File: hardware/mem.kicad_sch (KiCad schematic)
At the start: 4 parts, among them U11 AS6C4008-55PCN, U6 74HC00, U7 AT28LV256

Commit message: Changed Ethernet Chip to Ethernet ModuleWIZ850IO
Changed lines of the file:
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@@
-		)
-	)
-	(label "Bank_{2}"
-		(at 93.98 111.76 0)
-		(effects
-			(font
-				(size 1.27 1.27)
-			)
-			(justify left bottom)
 		)
 	)
@@
 		)
 	)
-	(label "Bank_{0}"
-		(at 231.14 104.14 0)
-		(effects
-			(font
-				(size 1.27 1.27)
-			)
-			(justify left bottom)
-		)
-	)
 	(label "D1"
 		(at 199.39 66.04 180)
@@
 		)
 	)
-	(label "Bank_{1}"
-		(at 231.14 106.68 0)
-		(effects
-			(font
-				(size 1.27 1.27)
-			)
-			(justify left bottom)
-		)
-	)
 	(label "D0"
 		(at 62.23 106.68 180)
@@
 		)
 	)
-	(label "Bank_{0}"
-		(at 93.98 106.68 0)
-		(effects
-			(font
-				(size 1.27 1.27)
-			)
-			(justify left bottom)
-		)
-	)
 	(label "D7"
 		(at 167.64 81.28 0)
@@
 		)
 	)
-	(label "Bank_{1}"
-		(at 93.98 109.22 0)
-		(effects
-			(font
-				(size 1.27 1.27)
-			)
-			(justify left bottom)
-		)
-	)
 	(label "Addr5"
 		(at 143.51 76.2 180)
@@
 	(label "D6"
 		(at 167.64 78.74 0)
-		(effects
-			(font
-				(size 1.27 1.27)
-			)
-			(justify left bottom)
-		)
-	)
-	(label "Bank_{2}"
-		(at 231.14 109.22 0)
 		(effects
 			(font
@@
 		)
 	)
+	(hierarchical_label "Bank_{0}"
+		(shape input)
+		(at 231.14 104.14 0)
+		(effects
+			(font
+				(size 1.27 1.27)
+			)
+			(justify left)
+		)
+	)
+	(hierarchical_label "Bank_{1}"
+		(shape input)
+		(at 93.98 109.22 0)
+		(effects
+			(font
+				(size 1.27 1.27)
+			)
+			(justify left)
+		)
+	)
+	(hierarchical_label "Bank_{2}"
+		(shape input)
+		(at 93.98 111.76 0)
+		(effects
+			(font
+				(size 1.27 1.27)
+			)
+			(justify left)
+		)
+	)
+	(hierarchical_label "Bank_{2}"
+		(shape input)
+		(at 231.14 109.22 0)
+		(effects
+			(font
+				(size 1.27 1.27)
+			)
+			(justify left)
+		)
+	)
+	(hierarchical_label "Bank_{0}"
+		(shape input)
+		(at 93.98 106.68 0)
+		(effects
+			(font
+				(size 1.27 1.27)
+			)
+			(justify left)
+		)
+	)
+	(hierarchical_label "Bank_{1}"
+		(shape input)
+		(at 231.14 106.68 0)
+		(effects
+			(font
+				(size 1.27 1.27)
+			)
+			(justify left)
+		)
+	)

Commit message: Fixes and addres fix adding VDA AND VPA
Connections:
- net PHI2 renamed CLK
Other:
- moved on the sheet: U6E
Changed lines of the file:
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@@
 	)
 	(junction
+		(at 77.47 140.97)
+		(diameter 0)
+		(color 0 0 0 0)
+	)
+	(junction
 		(at 135.89 132.08)
 		(diameter 0)
@@
 	(wire
 		(pts
+			(xy 60.96 140.97) (xy 77.47 140.97)
+		)
+		(stroke
+			(width 0)
+			(type default)
+		)
+	)
+	(wire
+		(pts
 			(xy 93.98 109.22) (xy 90.17 109.22)
 		)
@@
 		)
 	)
+	(wire
+		(pts
+			(xy 77.47 140.97) (xy 77.47 142.24)
+		)
+		(stroke
+			(width 0)
+			(type default)
+		)
+	)
 	(bus
 		(pts
@@
 	(wire
 		(pts
-			(xy 77.47 139.7) (xy 77.47 142.24)
+			(xy 77.47 139.7) (xy 77.47 140.97)
 		)
 		(stroke
@@
 		)
 	)
+	(wire
+		(pts
+			(xy 60.96 132.08) (xy 60.96 140.97)
+		)
+		(stroke
+			(width 0)
+			(type default)
+		)
+	)
 	(bus
 		(pts
@@
 		)
 	)
-	(global_label "PHI2"
+	(global_label "CLK"
 		(shape input)
 		(at 212.09 138.43 180)
@@
 		)
 		(property "Intersheetrefs" "${INTERSHEET_REFS}"
-			(at 204.69 138.43 0)
+			(at 205.5367 138.43 0)
 			(effects
 				(font
@@
 		)
 	)
-	(global_label "PHI2"
+	(global_label "CLK"
 		(shape input)
 		(at 35.56 134.62 180)
@@
 		)
 		(property "Intersheetrefs" "${INTERSHEET_REFS}"
-			(at 28.16 134.62 0)
+			(at 29.0067 134.62 0)
 			(effects
 				(font
@@
 		)
 	)
-	(global_label "PHI2"
+	(global_label "CLK"
 		(shape input)
 		(at 35.56 139.7 180)
@@
 		)
 		(property "Intersheetrefs" "${INTERSHEET_REFS}"
-			(at 28.16 139.7 0)
+			(at 29.0067 139.7 0)
 			(effects
 				(font
@@
 		)
 	)
-	(global_label "PHI2"
+	(global_label "CLK"
 		(shape input)
 		(at 119.38 129.54 180)
@@
 		)
 		(property "Intersheetrefs" "${INTERSHEET_REFS}"
-			(at 111.98 129.54 0)
+			(at 112.8267 129.54 0)
 			(effects
 				(font
@@
 	(symbol
 		(lib_id "74xx:74HC00")
-		(at 257.81 120.65 90)
+		(at 265.43 139.7 0)
 		(unit 5)
 		(exclude_from_sim no)
@@
 		(fields_autoplaced yes)
 		(property "Reference" "U6"
-			(at 257.81 110.49 90)
+			(at 275.59 139.7 90)
 			(effects
 				(font
@@
 		)
 		(property "Value" "74HC00"
-			(at 257.81 113.03 90)
+			(at 273.05 139.7 90)
 			(effects
 				(font
@@
 		)
 		(property "Footprint" "Package_DIP:DIP-14_W7.62mm"
-			(at 257.81 120.65 0)
+			(at 265.43 139.7 0)
 			(effects
 				(font
@@
 		)
 		(property "Datasheet" "http://www.ti.com/lit/gpn/sn74hc00"
-			(at 257.81 120.65 0)
+			(at 265.43 139.7 0)
 			(effects
 				(font
@@
 		)
 		(property "Description" "quad 2-input NAND gate"
-			(at 257.81 120.65 0)
+			(at 265.43 139.7 0)
 			(effects
 				(font
@@
 	(symbol
 		(lib_id "power:GND")
-		(at 270.51 120.65 90)
+		(at 265.43 152.4 0)
 		(unit 1)
 		(exclude_from_sim no)
@@
 		(dnp no)
 		(property "Reference" "#PWR022"
-			(at 276.86 120.65 0)
+			(at 265.43 158.75 0)
 			(effects
 				(font
@@
 		)
 		(property "Value" "GND"
-			(at 275.59 120.65 0)
+			(at 265.43 157.48 0)
 			(effects
 				(font
@@
 		)
 		(property "Footprint" ""
-			(at 270.51 120.65 0)
+			(at 265.43 152.4 0)
 			(effects
 				(font
@@
 		)
 		(property "Datasheet" ""
-			(at 270.51 120.65 0)
+			(at 265.43 152.4 0)
 			(effects
 				(font
@@
 		)
 		(property "Description" "Power symbol creates a global label with name \"GND\" , ground"
-			(at 270.51 120.65 0)
+			(at 265.43 152.4 0)
 			(effects
 				(font
@@
 	(symbol
 		(lib_id "power:+3.3V")
-		(at 142.24 104.14 90)
+		(at 142.24 104.14 0)
 		(unit 1)
 		(exclude_from_sim no)
@@
 		(dnp no)
 		(property "Reference" "#PWR024"
-			(at 146.05 104.14 0)
+			(at 142.24 107.95 0)
 			(effects
 				(font
@@
 		)
 		(property "Value" "+3.3V"
-			(at 137.16 104.14 90)
+			(at 141.986 100.584 0)
 			(effects
 				(font
@@
 	)
 	(symbol
-		(lib_id "power:GND")
-		(at 60.96 132.08 270)
-		(unit 1)
-		(exclude_from_sim no)
-		(in_bom yes)
-		(on_board yes)
-		(dnp no)
-		(fields_autoplaced yes)
-		(property "Reference" "#PWR04"
-			(at 54.61 132.08 0)
-			(effects
-				(font
-					(size 1.27 1.27)
-				)
-				(hide yes)
-			)
-		)
-		(property "Value" "GND"
-			(at 57.15 132.0799 90)
-			(effects
-				(font
-					(size 1.27 1.27)
-				)
-				(justify right)
-			)
-		)
-		(property "Footprint" ""
-			(at 60.96 132.08 0)
-			(effects
-				(font
-					(size 1.27 1.27)
-				)
-				(hide yes)
-			)
-		)
-		(property "Datasheet" ""
-			(at 60.96 132.08 0)
-			(effects
-				(font
-					(size 1.27 1.27)
-				)
-				(hide yes)
-			)
-		)
-		(property "Description" "Power symbol creates a global label with name \"GND\" , ground"
-			(at 60.96 132.08 0)
-			(effects
-				(font
-					(size 1.27 1.27)
-				)
-				(hide yes)
-			)
-		)
-		(pin "1"
-		)
-		(instances
-			(project "Lambda One"
-				(path "/73ea9964-373f-4fdc-b03e-f532cf836c0d/393dc2fd-ccc9-40ef-ba1b-4142573d9a3b"
-					(reference "#PWR04")
-					(unit 1)
-				)
-			)
-		)
-	)
-	(symbol
 		(lib_id "74xx:74HC00")
 		(at 43.18 137.16 0)
@@
 	(symbol
 		(lib_id "power:+3.3V")
-		(at 245.11 120.65 90)
+		(at 265.43 127 0)
 		(unit 1)
 		(exclude_from_sim no)
@@
 		(dnp no)
 		(property "Reference" "#PWR025"
-			(at 248.92 120.65 0)
+			(at 265.43 130.81 0)
 			(effects
 				(font
@@
 		)
 		(property "Value" "+3.3V"
-			(at 240.03 120.65 0)
+			(at 265.43 121.92 0)
 			(effects
 				(font
@@
 		)
 		(property "Footprint" ""
-			(at 245.11 120.65 0)
+			(at 265.43 127 0)
 			(effects
 				(font
@@
 		)
 		(property "Datasheet" ""
-			(at 245.11 120.65 0)
+			(at 265.43 127 0)
 			(effects
 				(font
@@
 		)
 		(property "Description" "Power symbol creates a global label with name \"+3.3V\""
-			(at 245.11 120.65 0)
+			(at 265.43 127 0)
 			(effects
 				(font

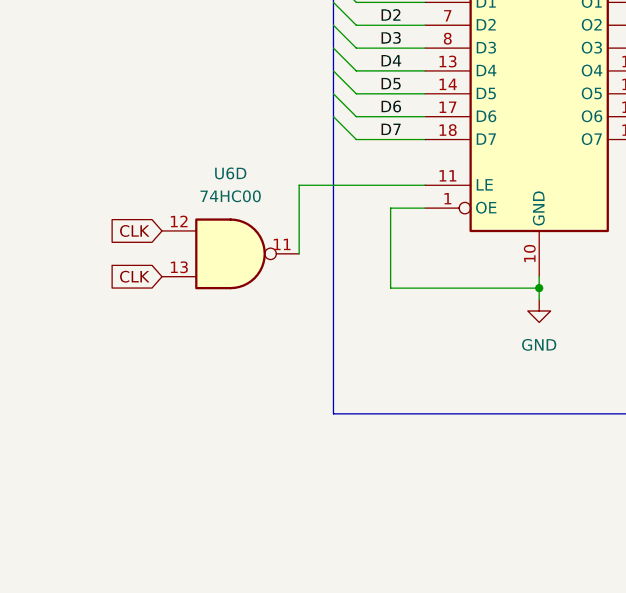
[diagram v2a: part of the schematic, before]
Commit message: Added Bus controller 74HC245
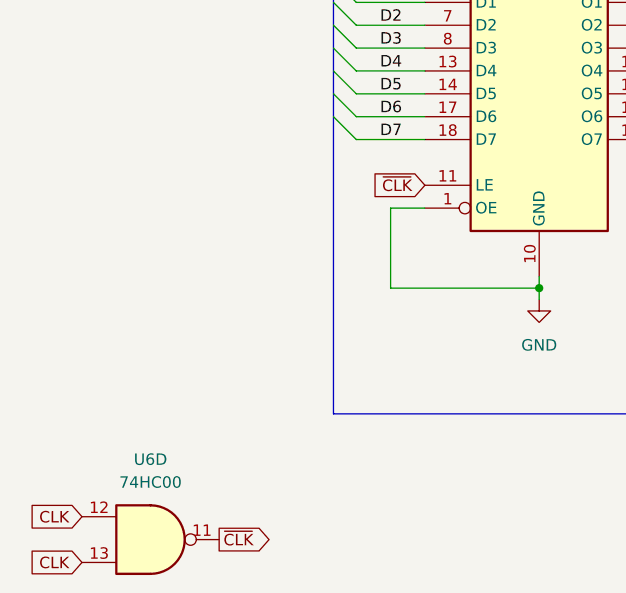
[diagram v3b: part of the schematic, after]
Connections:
- net ~{CLK}: now reaches BankRegister1.11 (LE), U6.11
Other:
- moved on the sheet: U6D
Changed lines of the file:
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@@
 	(wire
 		(pts
-			(xy 50.8 129.54) (xy 64.77 129.54)
-		)
-		(stroke
-			(width 0)
-			(type default)
-		)
-	)
-	(wire
-		(pts
 			(xy 135.89 132.08) (xy 135.89 118.11)
 		)
@@
 	(wire
 		(pts
-			(xy 50.8 129.54) (xy 50.8 137.16)
-		)
-		(stroke
-			(width 0)
-			(type default)
-		)
-	)
-	(wire
-		(pts
 			(xy 135.89 83.82) (xy 146.05 83.82)
 		)
@@
 		)
 	)
+	(global_label "~{CLK}"
+		(shape input)
+		(at 64.77 129.54 180)
+		(fields_autoplaced yes)
+		(effects
+			(font
+				(size 1.27 1.27)
+			)
+			(justify right)
+		)
+		(property "Intersheetrefs" "${INTERSHEET_REFS}"
+			(at 58.2167 129.54 0)
+			(effects
+				(font
+					(size 1.27 1.27)
+				)
+				(justify right)
+				(hide yes)
+			)
+		)
+	)
+	(global_label "~{CLK}"
+		(shape output)
+		(at 41.91 168.91 0)
+		(fields_autoplaced yes)
+		(effects
+			(font
+				(size 1.27 1.27)
+			)
+			(justify left)
+		)
+		(property "Intersheetrefs" "${INTERSHEET_REFS}"
+			(at 48.4633 168.91 0)
+			(effects
+				(font
+					(size 1.27 1.27)
+				)
+				(justify left)
+				(hide yes)
+			)
+		)
+	)
 	(global_label "R{slash}~{W}"
 		(shape input)
@@
 	(global_label "CLK"
 		(shape input)
-		(at 35.56 134.62 180)
+		(at 26.67 166.37 180)
 		(fields_autoplaced yes)
 		(effects
@@
 		)
 		(property "Intersheetrefs" "${INTERSHEET_REFS}"
-			(at 29.0067 134.62 0)
+			(at 20.1167 166.37 0)
 			(effects
 				(font
@@
 	(global_label "CLK"
 		(shape input)
-		(at 35.56 139.7 180)
+		(at 26.67 171.45 180)
 		(fields_autoplaced yes)
 		(effects
@@
 		)
 		(property "Intersheetrefs" "${INTERSHEET_REFS}"
-			(at 29.0067 139.7 0)
+			(at 20.1167 171.45 0)
 			(effects
 				(font
@@
 	(symbol
 		(lib_id "74xx:74HC00")
-		(at 43.18 137.16 0)
+		(at 34.29 168.91 0)
 		(unit 4)
 		(exclude_from_sim no)
@@
 		(fields_autoplaced yes)
 		(property "Reference" "U6"
-			(at 43.1717 128.27 0)
+			(at 34.2817 160.02 0)
 			(effects
 				(font
@@
 		)
 		(property "Value" "74HC00"
-			(at 43.1717 130.81 0)
+			(at 34.2817 162.56 0)
 			(effects
 				(font
@@
 		)
 		(property "Footprint" "Package_DIP:DIP-14_W7.62mm"
-			(at 43.18 137.16 0)
+			(at 34.29 168.91 0)
 			(effects
 				(font
@@
 		)
 		(property "Datasheet" "http://www.ti.com/lit/gpn/sn74hc00"
-			(at 43.18 137.16 0)
+			(at 34.29 168.91 0)
 			(effects
 				(font
@@
 		)
 		(property "Description" "quad 2-input NAND gate"
-			(at 43.18 137.16 0)
+			(at 34.29 168.91 0)
 			(effects
 				(font

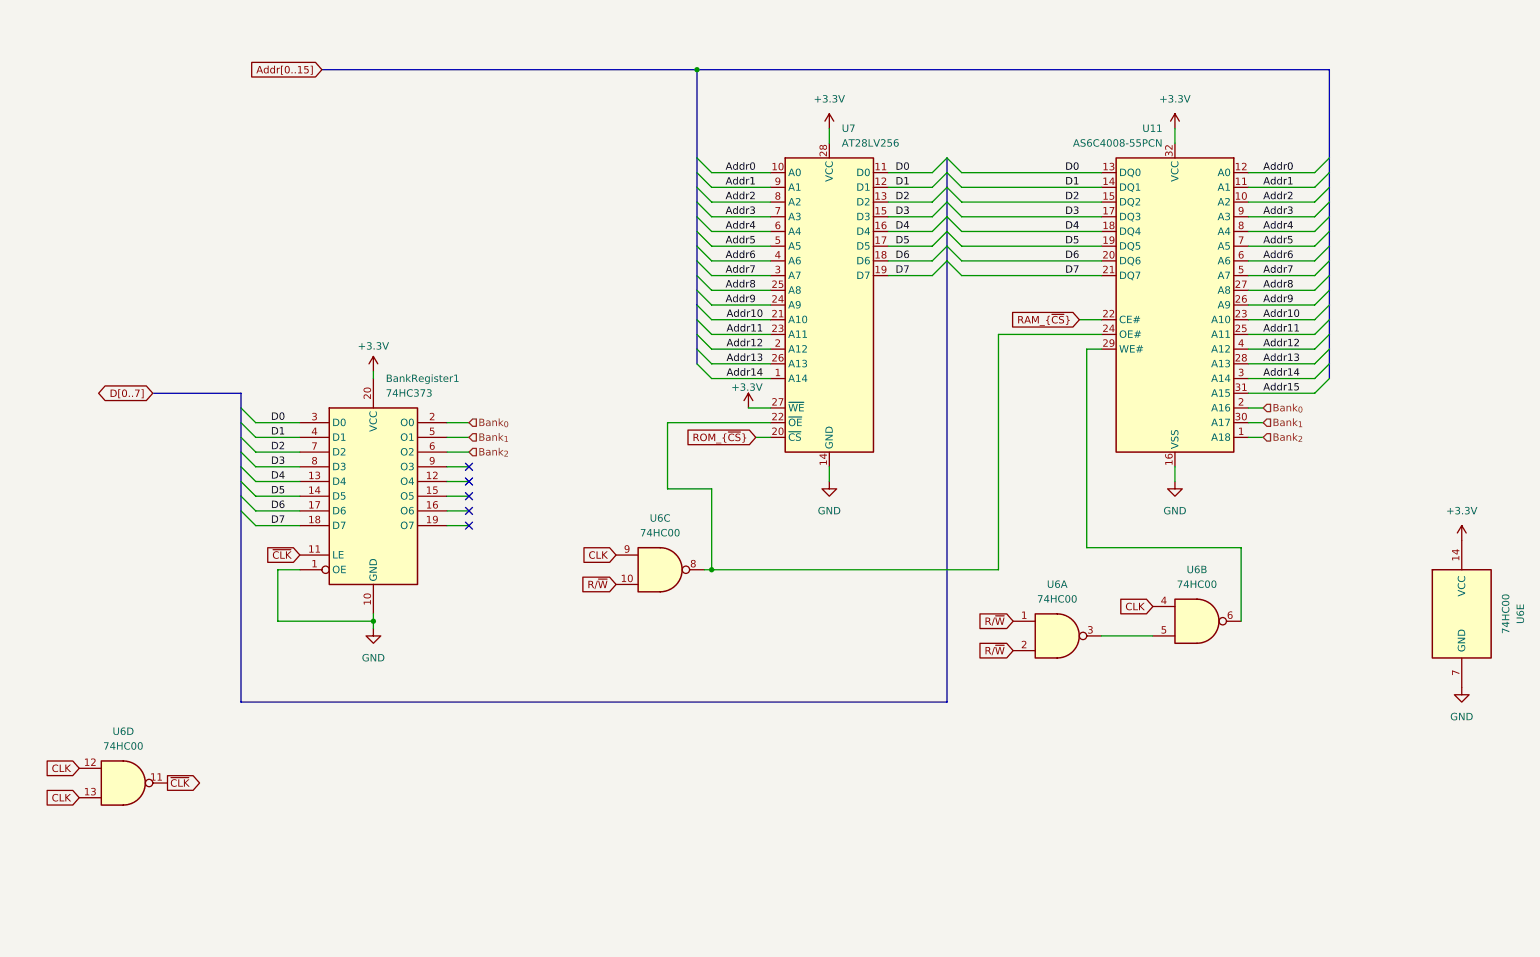
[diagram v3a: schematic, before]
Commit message: IMproved Serial With New CHIP, IMproved Video, Added external Serial Connections
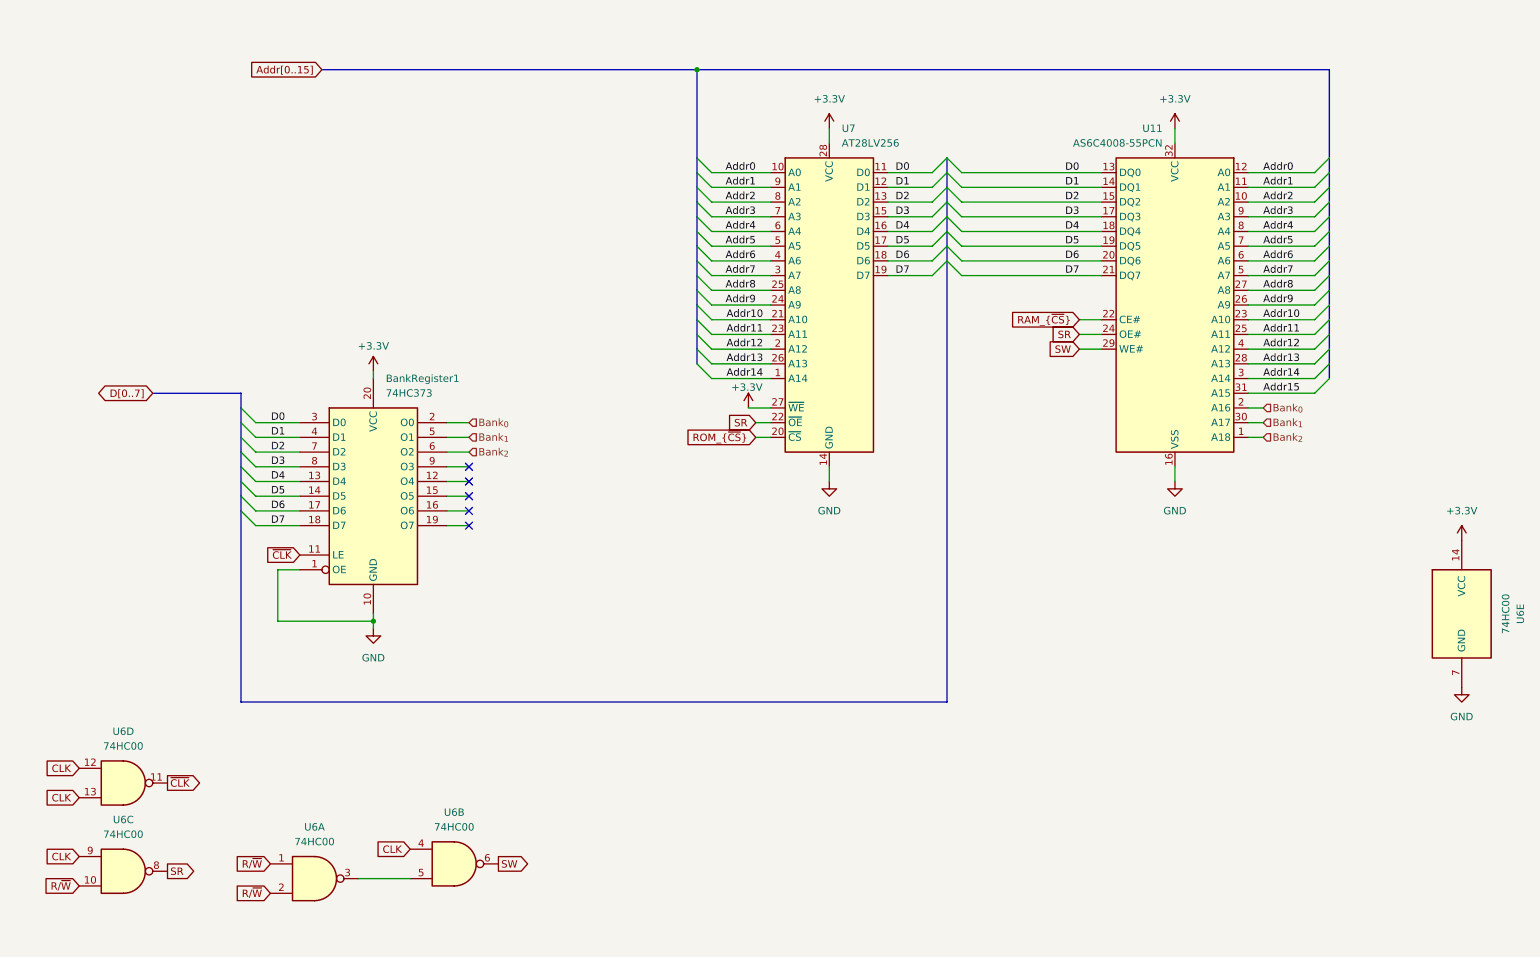
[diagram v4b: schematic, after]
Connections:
- net SR: now reaches U11.24 (OE#), U6.8, U7.22 (~{OE})
- net SW: now reaches U11.29 (WE#), U6.6

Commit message: Minor Improvemnts
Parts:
- U7: footprint AT28C256-15PU:DIP1544W45P254L3740H635Q28B -> Package_DIP:DIP-28_W15.24mm_Socket
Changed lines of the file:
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@@
 			)
 		)
-		(property "Footprint" "AT28C256-15PU:DIP1544W45P254L3740H635Q28B"
+		(property "Footprint" "Package_DIP:DIP-28_W15.24mm_Socket"
 			(at 156.21 86.36 0)
 			(effects

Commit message: PCD DESIGN
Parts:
- BankRegister1: footprint (none) -> Package_DIP:DIP-20_W7.62mm
- renumbered U11 to RAM1, U7 to ROM1
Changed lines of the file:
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@@
 		(on_board yes)
 		(dnp no)
-		(property "Reference" "U11"
+		(property "Reference" "RAM1"
 			(at 213.7567 55.88 0)
 			(effects
@@
 			(project "Lambda One"
 				(path "/73ea9964-373f-4fdc-b03e-f532cf836c0d/393dc2fd-ccc9-40ef-ba1b-4142573d9a3b"
-					(reference "U11")
+					(reference "RAM1")
 					(unit 1)
 				)
@@
 		(dnp no)
 		(fields_autoplaced yes)
-		(property "Reference" "U7"
+		(property "Reference" "ROM1"
 			(at 158.3533 55.88 0)
 			(effects
@@
 			(project "Lambda One"
 				(path "/73ea9964-373f-4fdc-b03e-f532cf836c0d/393dc2fd-ccc9-40ef-ba1b-4142573d9a3b"
-					(reference "U7")
+					(reference "ROM1")
 					(unit 1)
 				)
@@
 			)
 		)
-		(property "Footprint" ""
+		(property "Footprint" "Package_DIP:DIP-20_W7.62mm"
 			(at 77.47 119.38 0)
 			(effects
